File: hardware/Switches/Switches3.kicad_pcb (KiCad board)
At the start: 2 copper layers, 120 x 75 mm, 173 parts, among them J101 BusBar, J102 BusBar, J103 BusBar, J104 BusBar, J105 Conn_02x03_Odd_Even, Q101 IPT015N10N5, Q102 IPT015N10N5, Q103 IPT015N10N5, Q104 IPT015N10N5, Q105 IPT015N10N5, Q106 IPT015N10N5, Q107 IPT015N10N5, Q108 IPT015N10N5, Q109 IPT015N10N5, Q110 IPT015N10N5, Q111 IPT015N10N5, Q112 IPT015N10N5, U101 UCC27211DDAR, U102 UCC27211DDAR

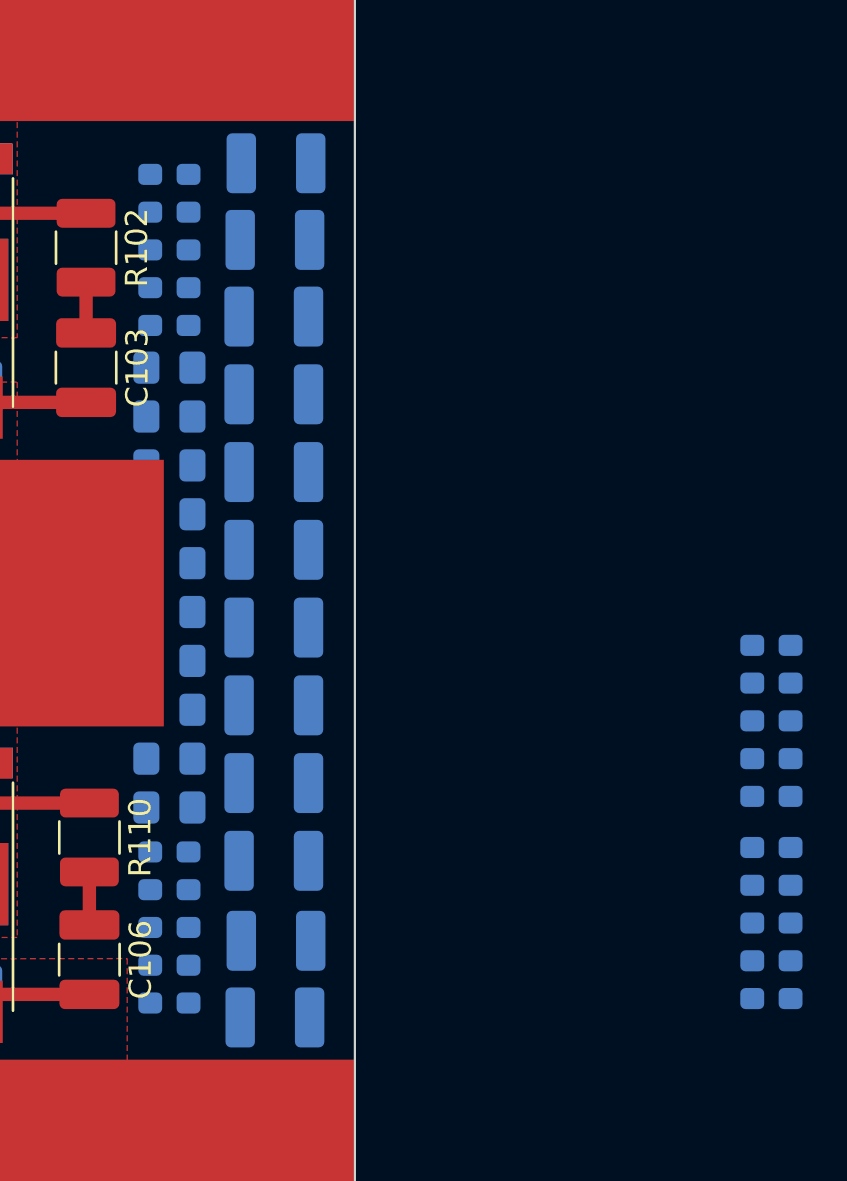
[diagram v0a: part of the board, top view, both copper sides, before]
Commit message: Driver and MOSFETs protections added, driver calculations done.
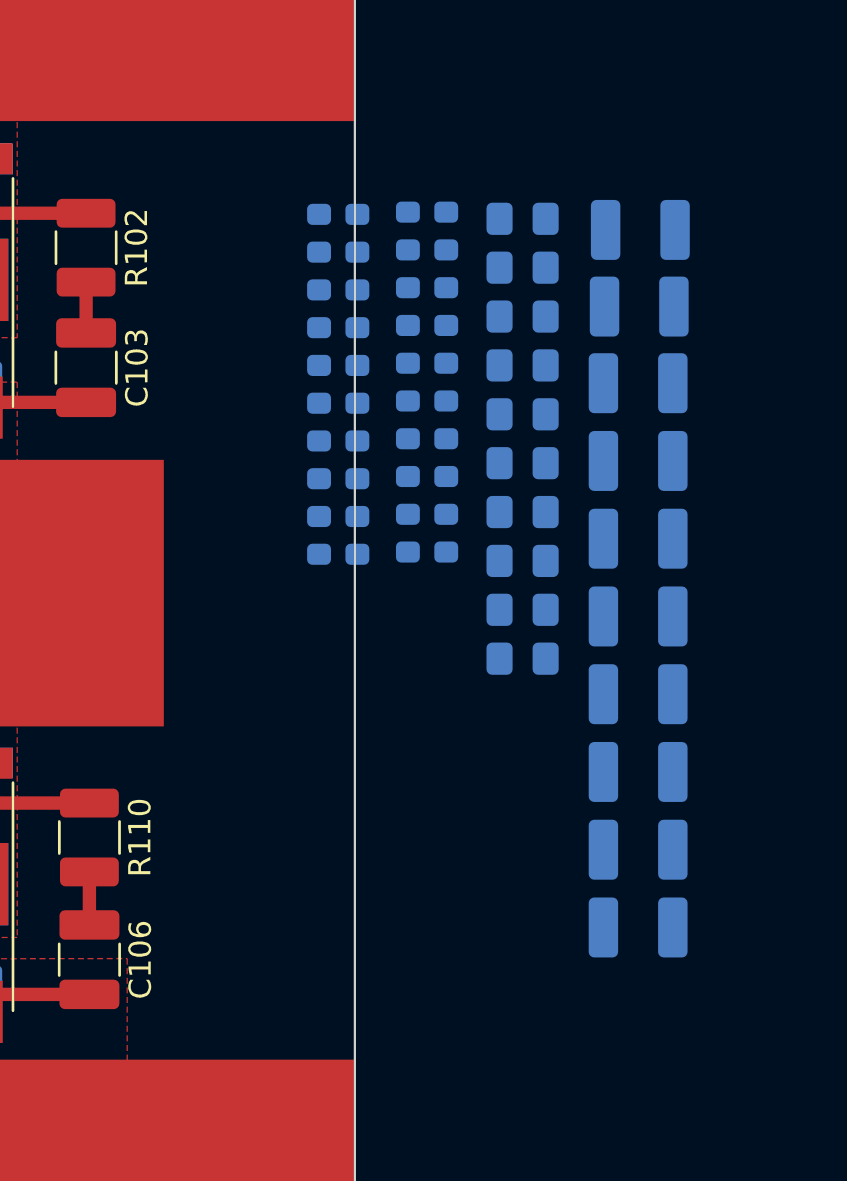
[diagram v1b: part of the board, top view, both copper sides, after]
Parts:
- removed the C120 at (218.7, 120.2)
- removed the C121 at (218.7, 116.7)
- removed the C121 at (218.7, 81.7)
- added C121: 10u, Capacitor_SMD:C_1210_3225Metric_Pad1.33x2.70mm_HandSolder, B.Cu at (235.1, 84.7)
- moved C173 31.0 mm to (225.5, 85.6)
- moved C170 31.0 mm to (225.5, 90.7)
- moved C171 31.0 mm to (225.5, 89.0)
- moved C172 31.0 mm to (225.5, 87.3)
- moved C174 31.0 mm to (225.5, 83.9)
- moved C185 27.9 mm to (221.5, 99.3)
- moved C186 27.9 mm to (221.5, 97.6)
- moved C187 27.9 mm to (221.5, 95.9)
- moved C188 27.9 mm to (221.5, 94.2)
- moved C189 27.9 mm to (221.5, 92.5)
- moved C165 19.0 mm to (225.5, 99.2)
- moved C166 19.0 mm to (225.5, 97.5)
- moved C167 19.0 mm to (225.5, 95.8)
- moved C168 19.0 mm to (225.5, 94.1)
- moved C169 19.0 mm to (225.5, 92.4)
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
